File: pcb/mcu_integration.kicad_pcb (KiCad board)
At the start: 4 copper layers, 70 x 70 mm, 67 parts, among them IC1 TL7660IDGKR, IC2 TL081IDT, IC6 AD844_OPAMP_AL, IC7 FOD814_OPTO_AL, J1 Conn_01x05, J4 Conn_01x02, J5 DM3BT-DSF-PEJS, M1 MountingHole_Pad, M2 MountingHole_Pad, M3 MountingHole_Pad, M4 MountingHole_Pad, U1 STM32F103RBTx, U3 REF192_AL, U6 LM35DM

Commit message: changed footprints and layout
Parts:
- removed J4: Conn_01x02, Connector_PinHeader_2.54mm:PinHeader_1x02_P2.54mm_Vertical
- C1: footprint Resistor_SMD:R_0402_1005Metric -> Capacitor_SMD:C_0402_1005Metric
- C12, C13, C22: footprint capstone:T495D -> Capacitor_SMD:C_0805_2012Metric
- C14, C15, C16, C17, C18, C43, C44, IC2, M1, M2, M3, M4, R10, R32, R5, R6, R7, R8, R9: moved to B.Cu
- C27, C33, I2C_1, IC6, IC7, J1, J_AD2, J_SIG1, PWR1, U1, U3: moved to F.Cu
- D2, D3: footprint Diode_SMD:D_0402_1005Metric -> capstone:SOD-323_1P7X1P25_ONS
- moved M4 63.4 mm to (173.2, 124.7), turned to 180 degrees
- moved M1 63.1 mm to (173.2, 68.7), turned to 180 degrees
- moved J1 59.4 mm to (171.2, 103.9), turned to 180 degrees
- moved R5 51.9 mm to (166.6, 117.0), turned to 180 degrees
- moved M2 51.3 mm to (117.2, 68.7), turned to 180 degrees
- moved M3 50.3 mm to (117.2, 124.7), turned to 180 degrees
- moved C14 50.2 mm to (166.0, 119.9)
- moved R3 48.4 mm to (167.2, 90.1), turned to 90 degrees
- moved R6 46.1 mm to (163.0, 117.1), turned to 180 degrees
- moved R4 46.0 mm to (167.2, 86.5)
- moved C9 44.8 mm to (151.0, 98.6), turned to 90 degrees
- moved C15 43.4 mm to (162.5, 119.9)
- moved I2C_1 42.9 mm to (171.2, 89.6), turned to 180 degrees
- moved C22 40.4 mm to (120.7, 101.0)
- moved R7 40.3 mm to (159.5, 117.1), turned to 180 degrees
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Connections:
- J_AD2 pad 3: ADC1_IN15_OPTO_E_AL -> ADC1_IN14_OPTO_F_AL
- J_AD2 pad 4: ADC1_IN14_OPTO_F_AL -> ADC1_IN15_OPTO_E_AL
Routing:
- net -5V Output: track 63.0 -> 118.0 mm, vias 4 -> 1
- net 3.3V Output: track 146.8 -> 96.1 mm, vias 6 -> 4
- net GND: track 110.4 -> 64.5 mm, vias 24 -> 37
- net ADC1_IN9_VREG_AL: track 46.8 -> 12.4 mm, vias 1 -> 0
- net RC_OUTPUT: track 50.0 -> 16.0 mm
- net /NRST: track 37.8 -> 20.2 mm, vias 1 -> 2
- net ADC1_IN0_SINE: track 98.2 -> 81.7 mm, vias 5 -> 1
- net /BOOT0: track 18.4 -> 2.48 mm, vias 1 -> 0
- net ADC1_IN14_OPTO_F_AL: track 30.6 -> 45.7 mm, vias 3 -> 2
- net ADC1_IN6_VREF_AL: track 29.0 -> 38.9 mm, vias 1 -> 2
- net Net-(J_SIG1-Pin_1): track 11.5 -> 19.8 mm
- net ADC1_IN3_OPAMP_AL: track 43.4 -> 50.6 mm, vias 3 -> 1
- net ADC1_IN15_OPTO_E_AL: track 45.9 -> 39.0 mm, vias 1 -> 0
- net +5V: track 29.8 -> 23.3 mm
- net Net-(U1-VDDA): track 11.6 -> 6.15 mm, vias 1 -> 0
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- added copper zone on In1.Cu, net +5V
- added copper zone on In2.Cu, net GND
- removed copper zone on In2.Cu, net +5V
- removed copper zone on In1.Cu, net GND
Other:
- board text added: "3.3V"
- board text added: "5V"
- board text added: "GND"
- board text added: "I2C_SCL"
- board text added: "I2C_SDA"
- board text added: "OPAMP"
- board text added: "OPTO_E"
- board text added: "OPTO_F"
- board text added: "RC"
- board text added: "SINE"
- board text added: "SQ"
- board text added: "VREF"

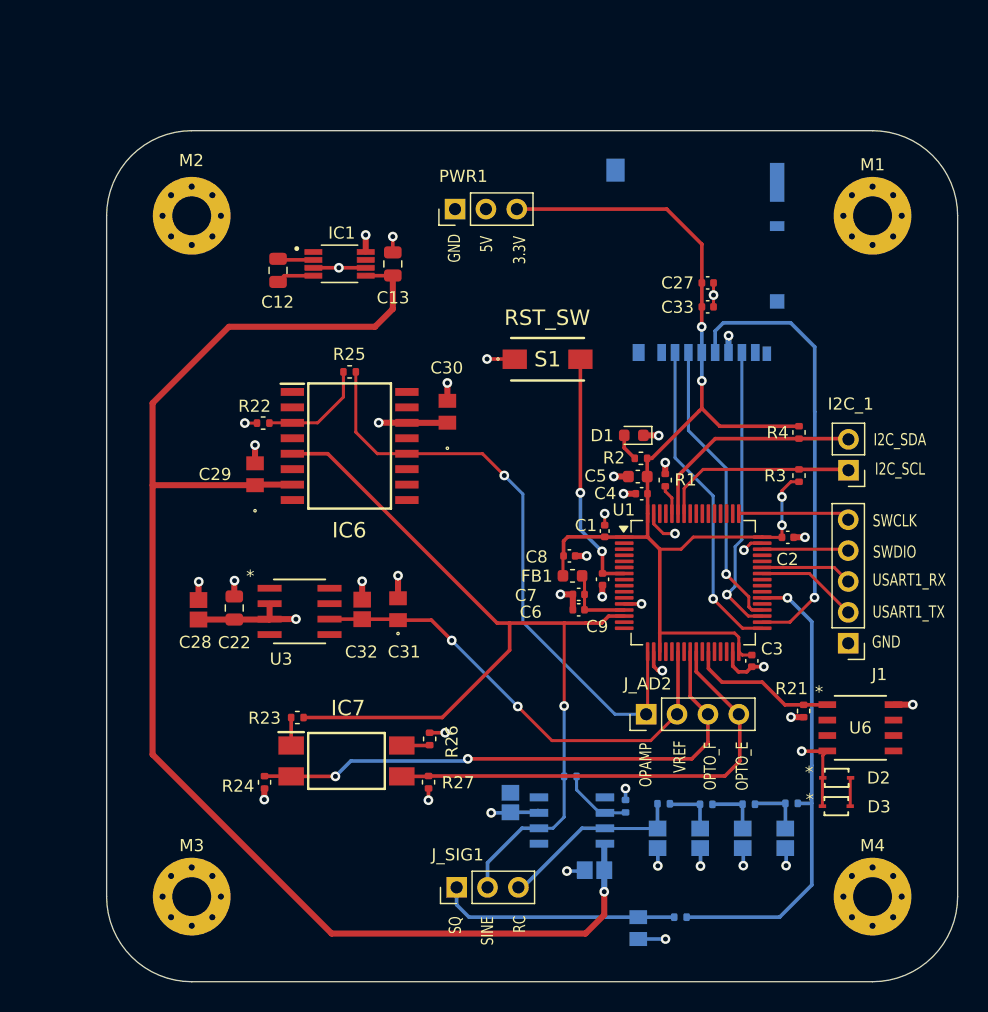
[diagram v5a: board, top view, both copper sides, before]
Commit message: Added Shields
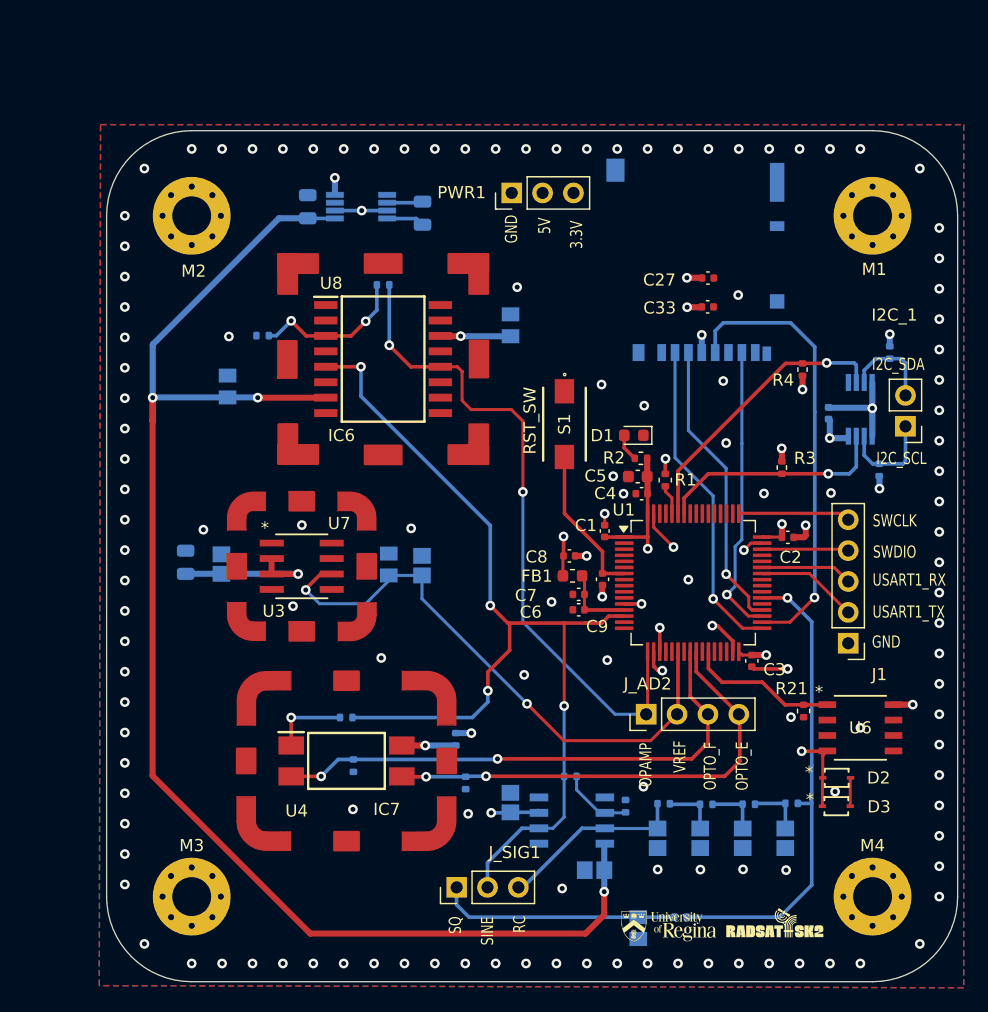
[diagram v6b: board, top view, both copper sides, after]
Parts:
- added C19: 10n, Capacitor_SMD:C_0402_1005Metric, B.Cu at (169.6, 84.9)
- added R11: 10K, Resistor_SMD:R_0402_1005Metric, B.Cu at (173.8, 89.6)
- added R12: 10K, Resistor_SMD:R_0402_1005Metric, B.Cu at (174.6, 79.9)
- added U2: LTC4300A-1IMS8_PBF, capstone:LTC4300A-1IMS8_PBF, B.Cu at (172.2, 84.6)
- added U4: FOD814_SHIELD, capstone:FOD814 Shield, F.Cu at (129.9, 113.5)
- added U7: REF192_SHIELD, capstone:REF192 Shield, F.Cu at (126.3, 97.5)
- added U8: AD844_SHIELD, capstone:AD844 Shield, F.Cu at (133.0, 80.5)
- C12, C13, C22, C28, C29, C30, C31, C32, IC1, R22, R23, R24, R25, R26, R27: moved to B.Cu
- R3, R4: value 2.2k -> 10K
- moved C12 12.8 mm to (136.2, 68.5)
- moved C30 8.81 mm to (143.4, 77.7)
- moved C13 8.43 mm to (126.8, 68.0)
- moved IC6 7.66 mm to (133.0, 80.5)
- moved R25 7.66 mm to (133.0, 74.4)
- moved C29 7.56 mm to (120.2, 82.7)
- moved R24 7.44 mm to (130.5, 113.9)
- moved R22 7.19 mm to (123.1, 78.6)
- moved C32 6.10 mm to (136.2, 97.5)
- moved I2C_1 5.92 mm to (175.9, 86.0)
- moved S1 5.52 mm to (147.9, 85.8), turned to -90 degrees
- moved C22 5.49 mm to (116.7, 97.2)
- moved R4 5.18 mm to (167.5, 81.3), turned to 90 degrees
- moved IC1 5.03 mm to (131.1, 67.9), turned to 180 degrees
- moved PWR1 4.85 mm to (143.5, 66.8)
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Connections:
- I2C_1 pad 1: OBC_I2C_SCL -> I2C_SCL
- I2C_1 pad 2: OBC_I2C_SDA -> I2C_SDA
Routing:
- net 3.3V Output: track 96.1 -> 44.0 mm, vias 4 -> 13
- net GND: track 64.5 -> 35.5 mm, vias 37 -> 141
- net ADC1_IN6_VREF_AL: track 38.9 -> 48.2 mm
- net I2C_SCL: track 0.00 -> 8.23 mm
- net I2C_SDA: track 0.00 -> 7.61 mm
- net /NRST: track 20.2 -> 12.7 mm, vias 2 -> 0
- net ADC1_IN3_OPAMP_AL: track 50.6 -> 55.8 mm, vias 1 -> 2
- net OBC_I2C_SDA: track 18.5 -> 23.4 mm, vias 0 -> 1
- net Net-(IC7-AK): track 2.30 -> 6.32 mm, vias 0 -> 1
- net Net-(IC6--IN): track 9.02 -> 12.9 mm, vias 0 -> 2
- net +5V: track 23.3 -> 26.8 mm
- net ADC1_IN0_SINE: track 81.7 -> 84.6 mm, vias 1 -> 4
- net OBC_I2C_SCL: track 16.3 -> 19.0 mm, vias 0 -> 1
- net Net-(IC7-C): track 2.26 -> 4.44 mm, vias 0 -> 1
- net ADC1_IN14_OPTO_F_AL: track 45.7 -> 43.5 mm
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- added copper zone on In2.Cu, net +5V
- added copper zone on In2.Cu, net 3.3V Output
- added copper zone on B.Cu, net GND
- added copper zone on F.Cu, net GND
- added copper zone on In1.Cu, net GND
- removed copper zone on In1.Cu, net +5V
- removed copper zone on In2.Cu, net GND
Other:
- board text added: "Minature Analog Payload REV A Owen Markewich Hunter Gerbrandt"

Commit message: Adjusted Silkscreen
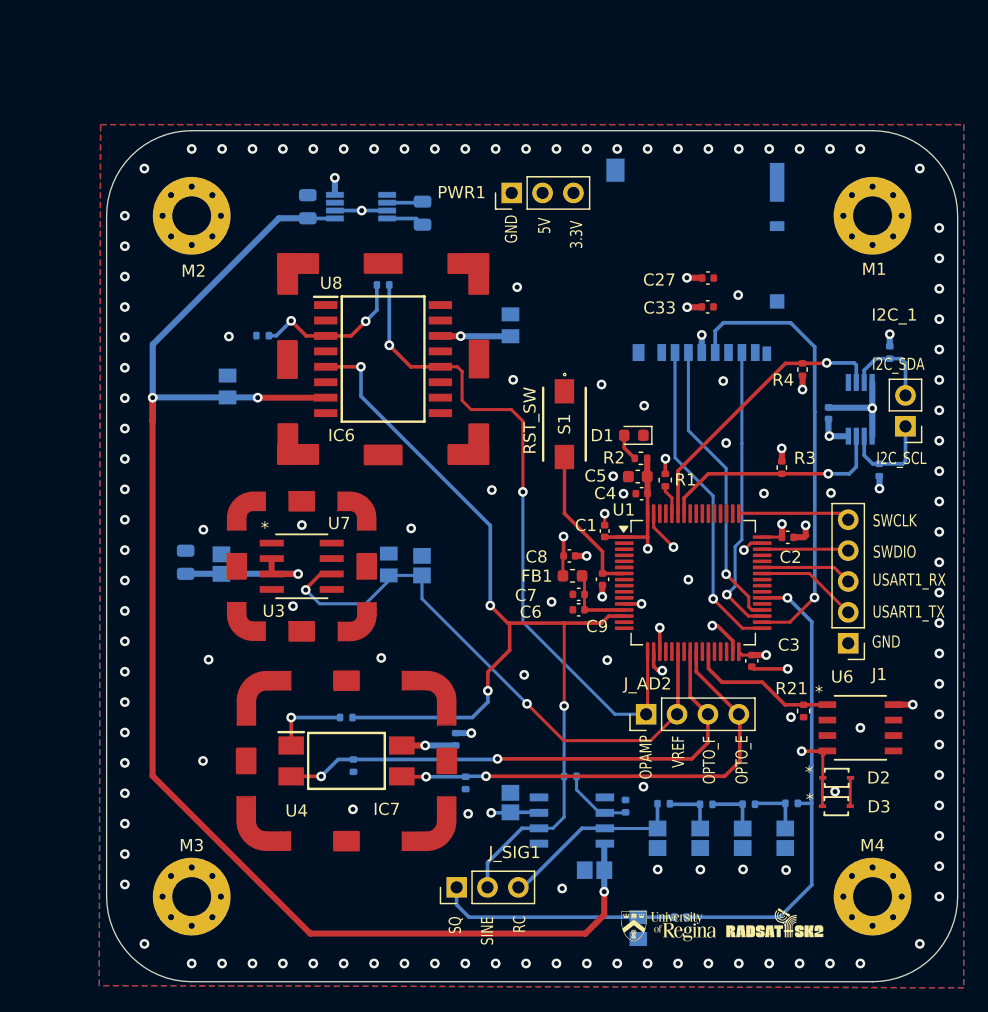
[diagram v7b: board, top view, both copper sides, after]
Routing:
- net GND: track 35.5 -> 35.3 mm, vias 141 -> 145
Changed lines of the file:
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@@
 		(tags "LM35DM ")
 		(property "Reference" "U6"
-			(at 0 0 0)
+			(at -1.501348 -4.185 0)
 			(unlocked yes)
 			(layer "F.SilkS")
@@
 		)
 		(fp_text user "${REFERENCE}"
-			(at 0 0 0)
+			(at 0 1.695 0)
 			(unlocked yes)
 			(layer "F.Fab")
@@
 		(tags "capacitor")
 		(property "Reference" "C3"
-			(at 0.72 -1.86 0)
+			(at -1.3 -3.05 0)
 			(layer "F.SilkS")
 			(effects
@@
 	)
 	(gr_text "OPAMP"
-		(at 155.15 115.69 90)
+		(at 155.17 115.06 90)
 		(layer "F.SilkS")
 		(effects
@@
 	)
 	(gr_text "OPTO_E"
-		(at 163.08 115.98 90)
+		(at 163.06 115.46 90)
 		(layer "F.SilkS")
 		(effects
@@
 	)
 	(gr_text "OPTO_F"
-		(at 160.45 115.95 90)
+		(at 160.38 115.46 90)
 		(layer "F.SilkS")
 		(effects
@@
 	)
 	(gr_text "VREF"
-		(at 157.95 114.53 90)
+		(at 157.84 114.12 90)
 		(layer "F.SilkS")
 		(effects
@@
 	)
 	(via
+		(at 143.66 82.19)
+		(size 0.8)
+		(drill 0.4)
+		(layers "F.Cu" "B.Cu")
+		(free yes)
+		(net 86)
+	)
+	(via
 		(at 170.14 116.06)
 		(size 0.8)
@@
 	)
 	(via
+		(at 118.15 113.54)
+		(size 0.8)
+		(drill 0.4)
+		(layers "F.Cu" "B.Cu")
+		(free yes)
+		(net 86)
+	)
+	(via
 		(at 167.39 112.74)
 		(size 0.8)
@@
 	)
 	(via
+		(at 141.91 91.26)
+		(size 0.8)
+		(drill 0.4)
+		(layers "F.Cu" "B.Cu")
+		(free yes)
+		(net 86)
+	)
+	(via
 		(at 178.71 122.2)
 		(size 0.8)
@@
 	)
 	(via
-		(at 169.7 86.99)
+		(at 169.67 86.82)
 		(size 0.8)
 		(drill 0.4)
@@
 	)
 	(via
+		(at 118.61 105.21)
+		(size 0.8)
+		(drill 0.4)
+		(layers "F.Cu" "B.Cu")
+		(free yes)
+		(net 86)
+	)
+	(via
 		(at 135.27 94.41)
 		(size 0.8)
@@
 	)
 	(segment
+		(start 169.76 86.82)
+		(end 169.77 86.83)
+		(width 0.5)
+		(layer "B.Cu")
+		(net 86)
+	)
+	(segment
+		(start 169.67 86.82)
+		(end 169.76 86.82)
+		(width 0.5)
+		(layer "B.Cu")
+		(net 86)
+	)
+	(segment
 		(start 149.468904 122.6)
 		(end 149.548904 122.52)
@@
 	)
 	(segment
-		(start 171.2181 86.8467)
-		(end 171.2181 86.8298)
-		(width 0.5)
-		(layer "B.Cu")
-		(net 86)
-	)
-	(segment
 		(start 155.56 120.723895)
 		(end 155.541703 120.705598)
@@
 	)
 	(segment
-		(start 169.7 86.99)
-		(end 169.7 85.52)
+		(start 171.2014 86.83)
+		(end 171.2181 86.8467)
 		(width 0.5)
 		(layer "B.Cu")
@@
 	)
 	(segment
-		(start 171.0748 86.99)
-		(end 171.2181 86.8467)
+		(start 169.77 86.83)
+		(end 171.2014 86.83)
 		(width 0.5)
 		(layer "B.Cu")
@@
 	)
 	(segment
+		(start 169.6 86.75)
+		(end 169.6 85.42)
+		(width 0.5)
+		(layer "B.Cu")
+		(net 86)
+	)
+	(segment
 		(start 171.1748 86.89)
 		(end 171.235 86.8298)
@@
 	)
 	(segment
-		(start 131.2 68.27)
-		(end 128.995 68.27)
-		(width 0.3)
+		(start 169.67 86.82)
+		(end 169.6 86.75)
+		(width 0.5)
 		(layer "B.Cu")
 		(net 86)
 	)
 	(segment
-		(start 169.7 85.52)
-		(end 169.6 85.42)
-		(width 0.5)
+		(start 131.2 68.27)
+		(end 128.995 68.27)
+		(width 0.3)
 		(layer "B.Cu")
 		(net 86)
 	)
 	(segment
-		(start 169.7 86.99)
-		(end 171.0748 86.99)
+		(start 171.2181 86.8467)
+		(end 171.2181 86.8298)
 		(width 0.5)
 		(layer "B.Cu")

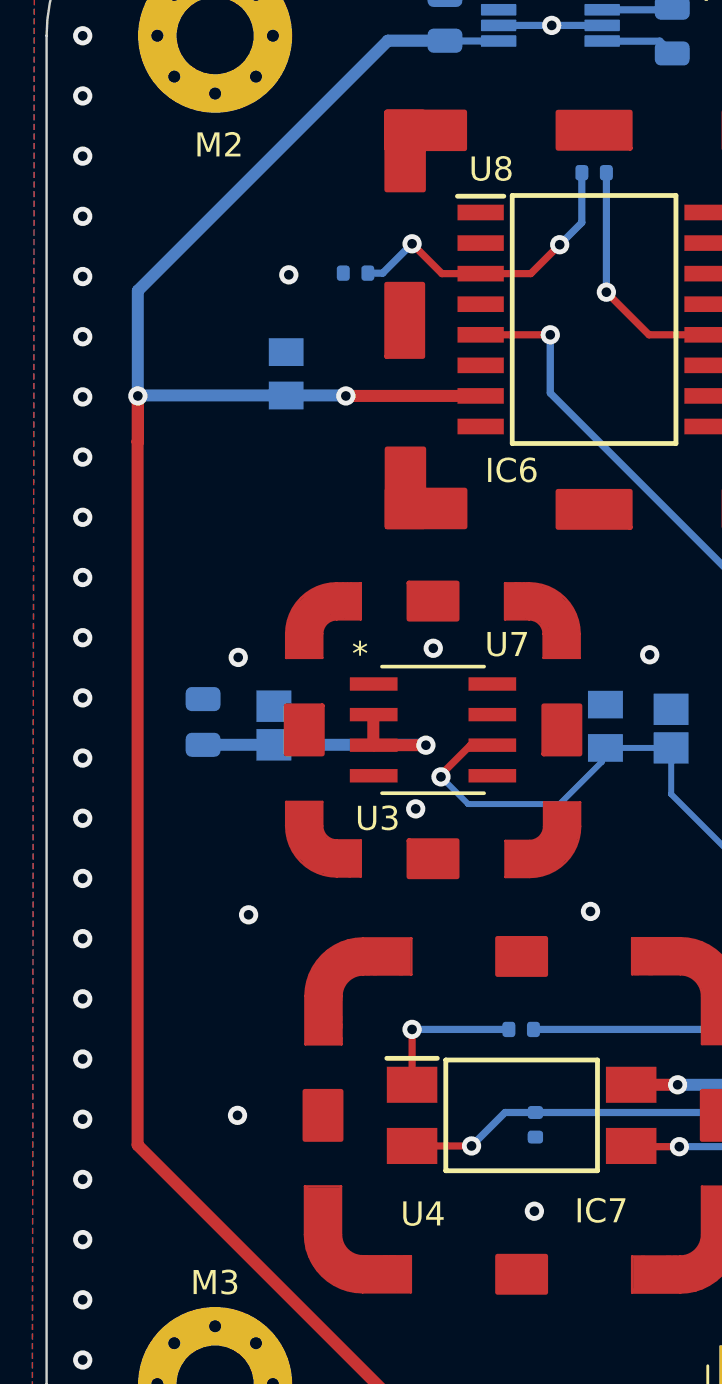
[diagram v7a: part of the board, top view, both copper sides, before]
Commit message: Fixed Footprints
-Added Solder Mask
-Symbol Pin Numbers
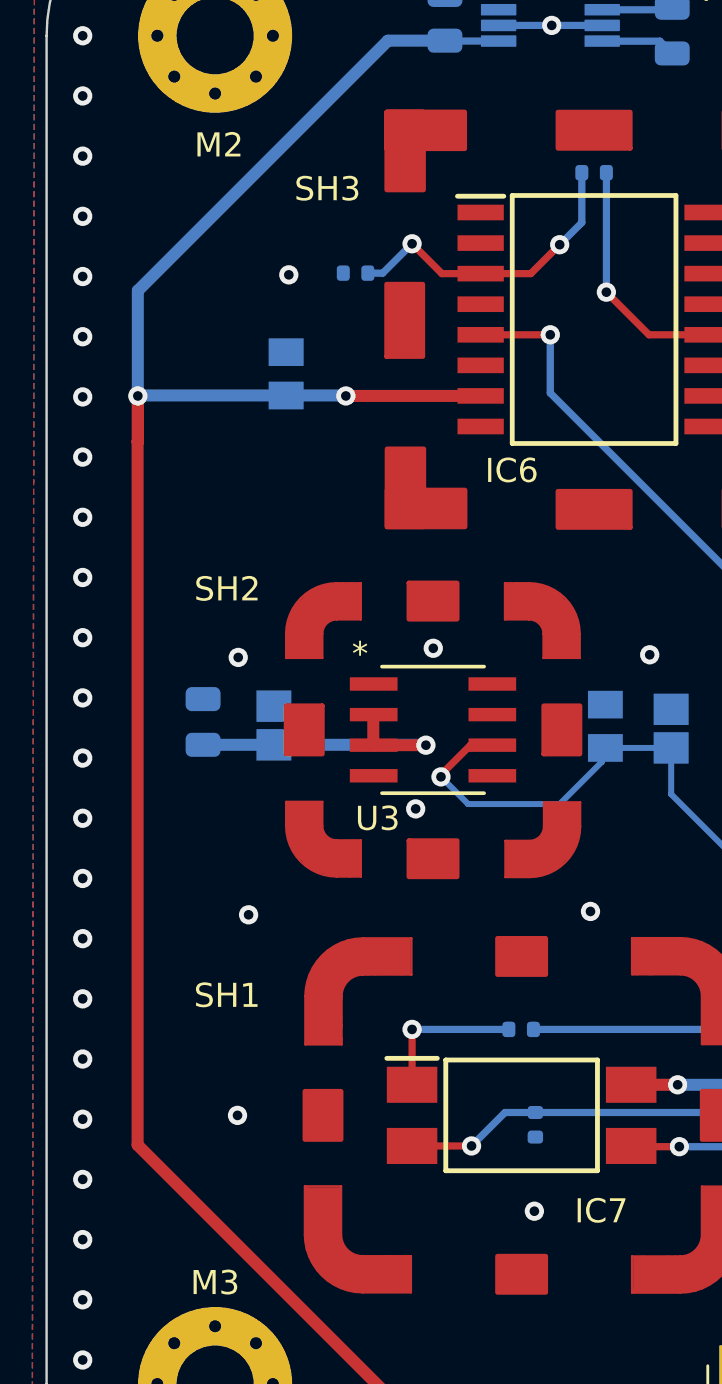
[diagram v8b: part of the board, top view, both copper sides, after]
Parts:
- removed U4: FOD814_SHIELD, capstone:FOD814 Shield
- removed U7: REF192_SHIELD, capstone:REF192 Shield
- removed U8: AD844_SHIELD, capstone:AD844 Shield
- added SH1: FOD814_SHIELD, capstone:FOD814 Shield, F.Cu at (129.9, 113.5)
- added SH2: REF192_SHIELD, capstone:REF192 Shield, F.Cu at (126.3, 97.5)
- added SH3: AD844_SHIELD, capstone:AD844 Shield, F.Cu at (133.0, 80.5)
